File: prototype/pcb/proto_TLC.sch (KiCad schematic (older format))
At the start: 21 parts, among them U1 TLC5954

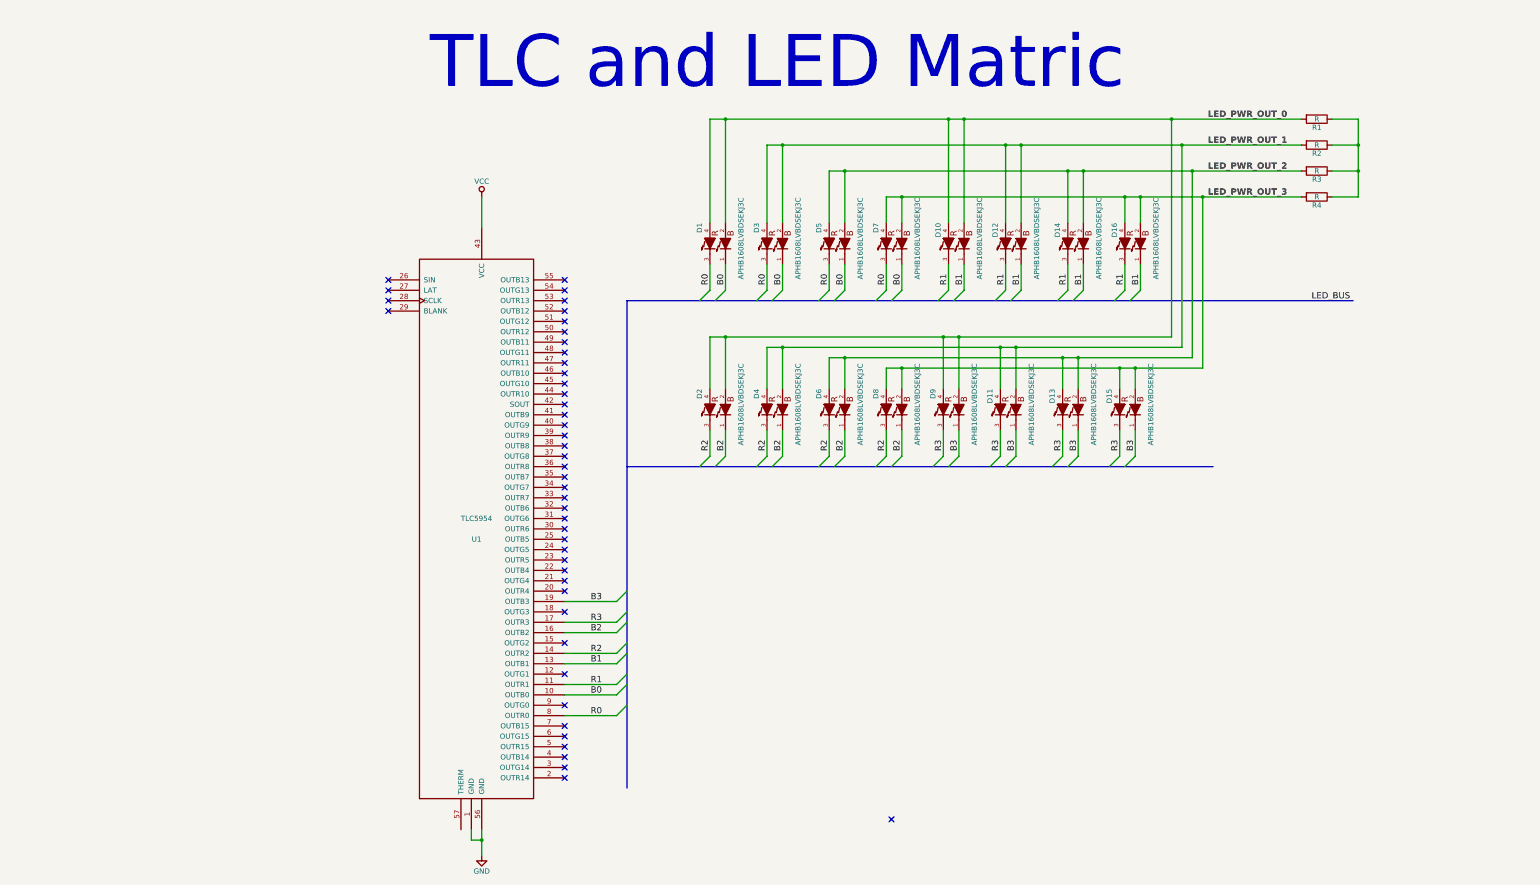
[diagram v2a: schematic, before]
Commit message: Added connectors, power mosfets, hierarchial pins
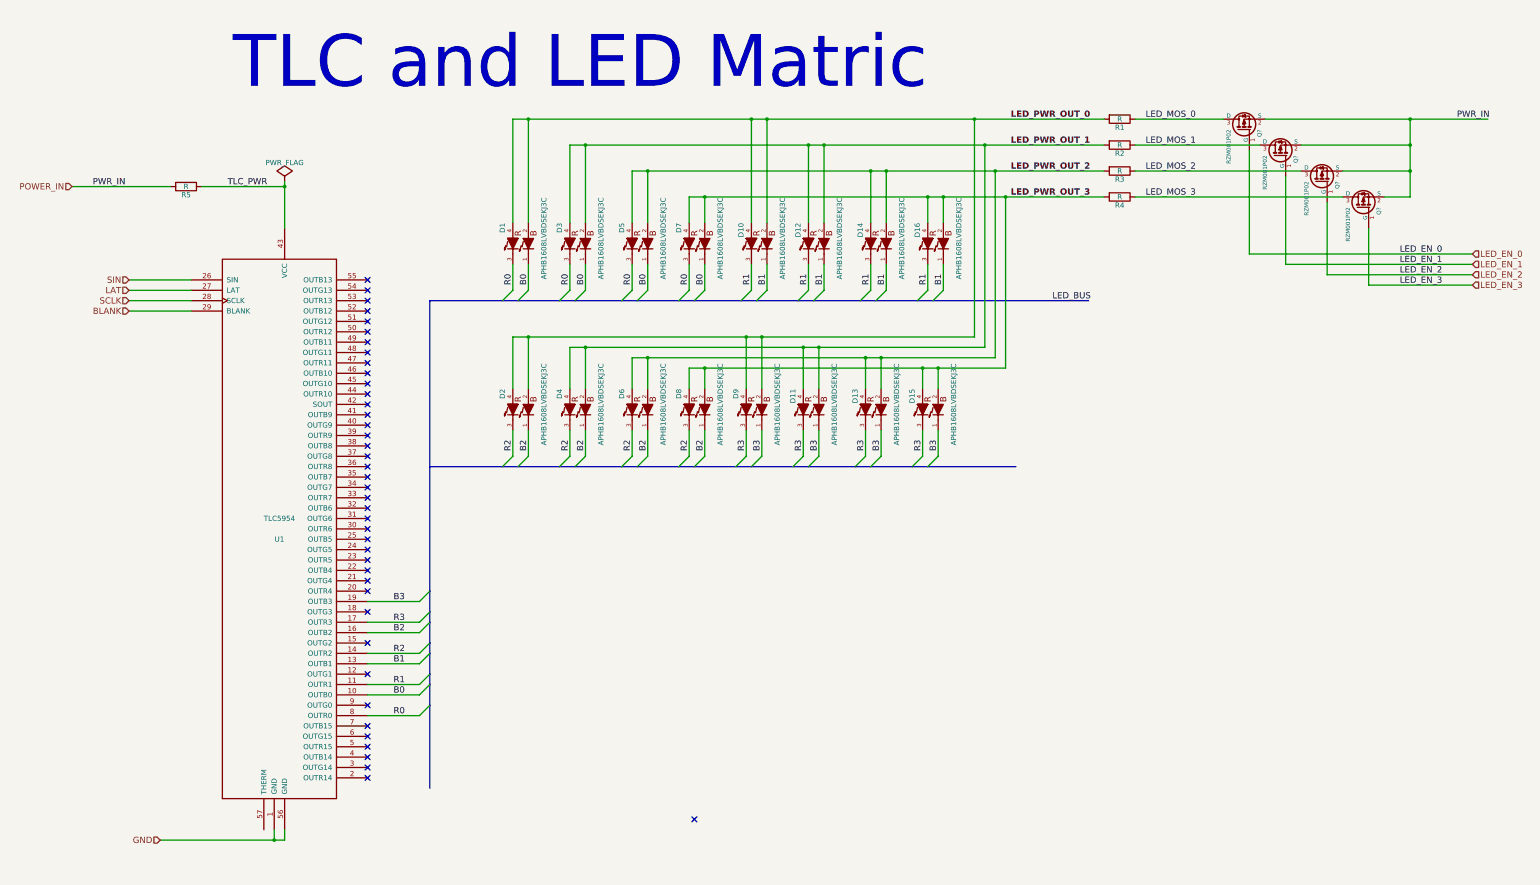
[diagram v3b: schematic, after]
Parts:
- added Q? (x4): RZM001P02, TO220, symbol RZM001P02
- added R5: R, symbol R
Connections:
- net SIN: now reaches U1.26 (SIN)
- net LAT: now reaches U1.27 (LAT)
- net SCLK: now reaches U1.28 (SCLK)
- net BLANK: now reaches U1.29 (BLANK)
- net VCC renamed TLC_PWR
- net TLC_PWR: now also R5.1
- new net LED_EN_0: Q?.1 (G)
- new net LED_EN_1: Q?.1 (G)
- new net LED_EN_2: Q?.1 (G)
- new net LED_EN_3: Q?.1 (G)
- new net LED_MOS_0: Q?.3 (D), R1.1
- new net LED_MOS_1: Q?.3 (D), R2.1
- new net LED_MOS_2: Q?.3 (D), R3.1
- new net LED_MOS_3: Q?.3 (D), R4.1
- new net POWER_IN: Q?.2 (S), Q?.2 (S), Q?.2 (S), Q?.2 (S), R5.2
- no-connect marks 46 -> 42
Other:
- moved on the sheet: D1, D10, D11, D12, D13, D14, D15, D16, D2, D3, D4, D5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

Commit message: Generate schematic pdf
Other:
- note added: "TLC and LED Matrix"
- note removed: "TLC and LED Matric"
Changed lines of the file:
@@
 $EndDescr
 Text Notes 3250 1400 0    500  ~ 0
-TLC and LED Matric
+TLC and LED Matrix
 $Comp
 L TLC5954 U1

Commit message: Bulk caps for TLC / LEDs
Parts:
- added C? (x3): C, symbol C
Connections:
- net GND: now also C?.2, C?.2, C?.2
- net POWER_IN: now also C?.1
- net TLC_PWR: now also C?.1, C?.1
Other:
- moved on the sheet: R5

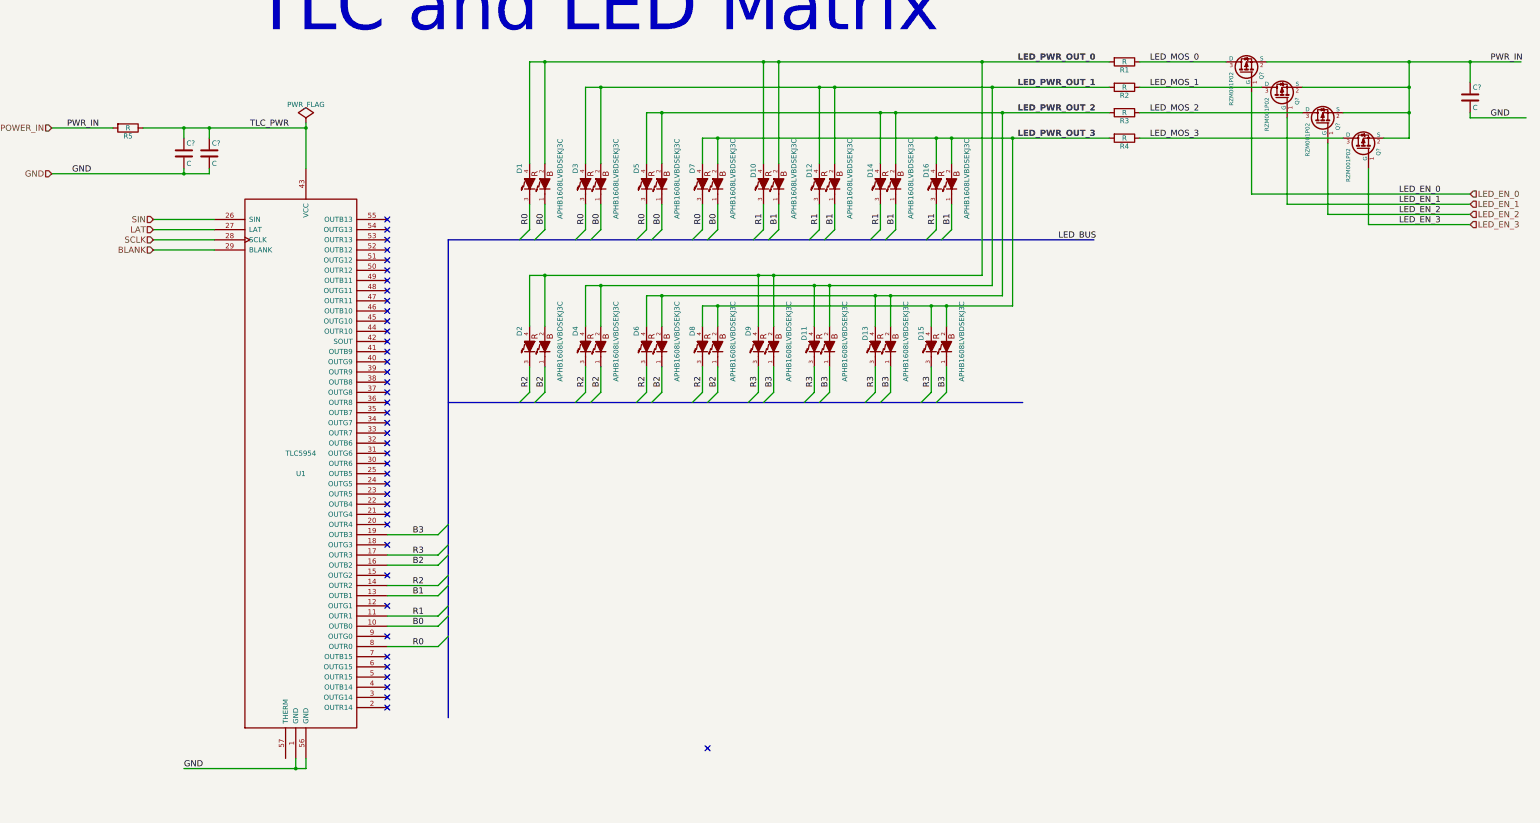
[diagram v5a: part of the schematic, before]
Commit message: Finished footprints and netlist
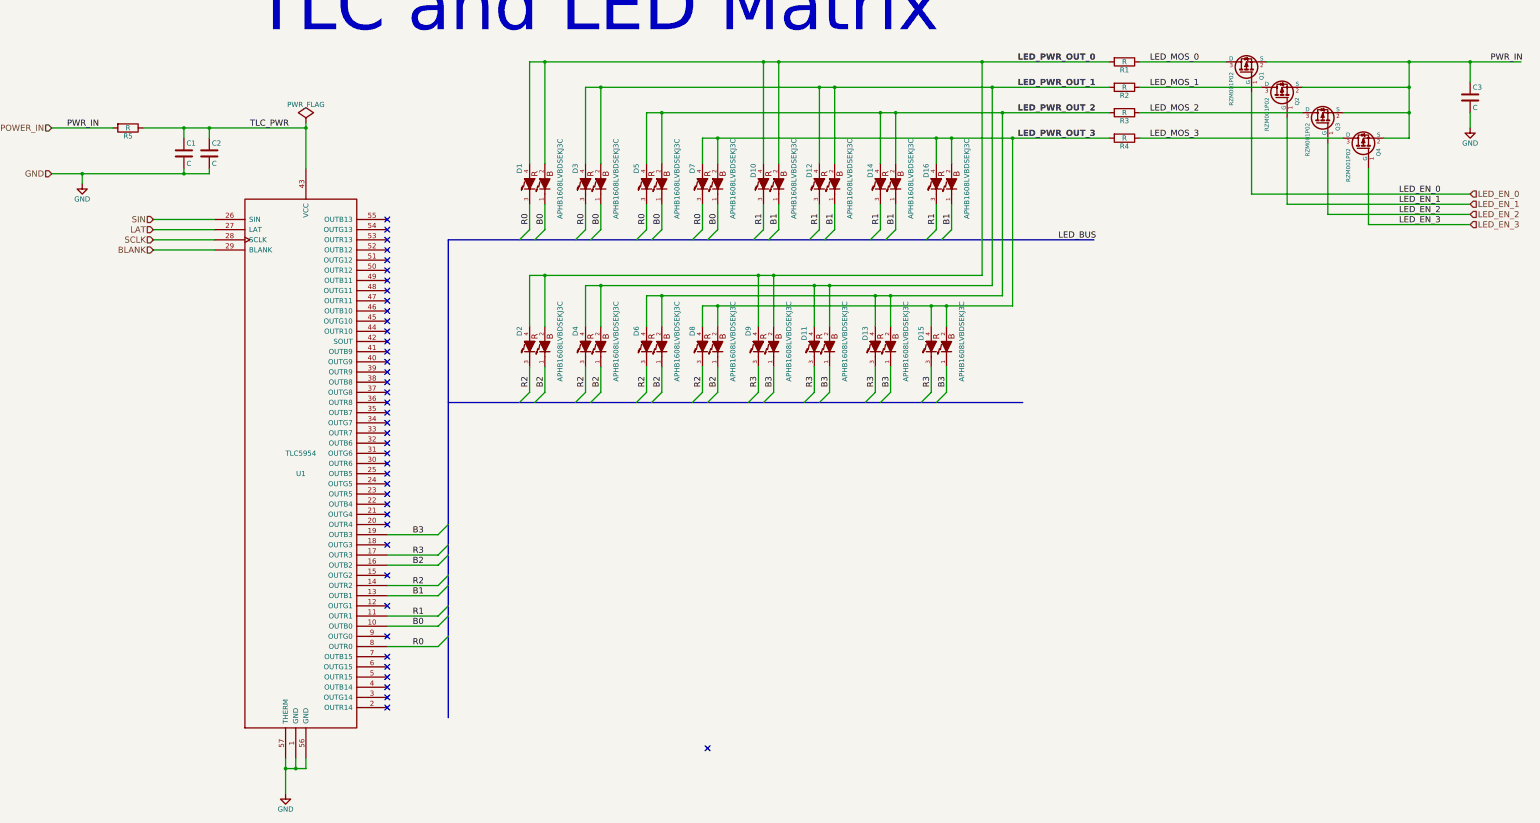
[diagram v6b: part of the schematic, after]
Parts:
- C1, C2, C3: renamed from C?; footprint (none) -> Capacitors_SMD:C_0603
- D1, D10, D11, D12, D13, D14, D15, D16, D2, D3, D4, D5, D6, D7, D8, D9: footprint (none) -> led:led_dual
- Q1, Q2, Q3, Q4: renamed from Q?; footprint TO220 -> smt:SOT-723-3
- R1, R2, R3, R4, R5: footprint (none) -> Resistors_SMD:R_0603
- U1: footprint MODULE -> smt:QFN_N56_THERM
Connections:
- net GND: now also U1.57 (THERM)
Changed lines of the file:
@@
 F 0 "U1" H 3700 5500 50  0000 C CNN
 F 1 "TLC5954" H 3700 5700 50  0000 C CNN
-F 2 "MODULE" H 3700 5600 50  0001 C CNN
+F 2 "smt:QFN_N56_THERM" H 3700 5600 50  0001 C CNN
 F 3 "DOCUMENTATION" H 3700 5600 50  0001 C CNN
 	1    3700 5600
@@
 F 0 "D1" H 5850 3050 50  0000 L CNN
 F 1 "APHB1608LVBDSEKJ3C" H 6000 2650 50  0000 C CNN
-F 2 "" H 6050 2800 60  0000 C CNN
+F 2 "led:led_dual" H 6050 2800 60  0001 C CNN
 F 3 "" H 6050 2800 60  0000 C CNN
 	1    6050 2850
@@
 F 0 "D3" H 6400 3050 50  0000 L CNN
 F 1 "APHB1608LVBDSEKJ3C" H 6550 2650 50  0000 C CNN
-F 2 "" H 6600 2800 60  0000 C CNN
+F 2 "led:led_dual" H 6600 2800 60  0001 C CNN
 F 3 "" H 6600 2800 60  0000 C CNN
 	1    6600 2850
@@
 F 0 "D5" H 7000 3050 50  0000 L CNN
 F 1 "APHB1608LVBDSEKJ3C" H 7150 2650 50  0000 C CNN
-F 2 "" H 7200 2800 60  0000 C CNN
+F 2 "led:led_dual" H 7200 2800 60  0001 C CNN
 F 3 "" H 7200 2800 60  0000 C CNN
 	1    7200 2850
@@
 F 0 "D7" H 7550 3050 50  0000 L CNN
 F 1 "APHB1608LVBDSEKJ3C" H 7700 2650 50  0000 C CNN
-F 2 "" H 7750 2800 60  0000 C CNN
+F 2 "led:led_dual" H 7750 2800 60  0001 C CNN
 F 3 "" H 7750 2800 60  0000 C CNN
 	1    7750 2850
@@
 F 0 "D10" H 8150 3050 50  0000 L CNN
 F 1 "APHB1608LVBDSEKJ3C" H 8300 2650 50  0000 C CNN
-F 2 "" H 8350 2800 60  0000 C CNN
+F 2 "led:led_dual" H 8350 2800 60  0001 C CNN
 F 3 "" H 8350 2800 60  0000 C CNN
 	1    8350 2850
@@
 F 0 "D12" H 8700 3050 50  0000 L CNN
 F 1 "APHB1608LVBDSEKJ3C" H 8850 2650 50  0000 C CNN
-F 2 "" H 8900 2800 60  0000 C CNN
+F 2 "led:led_dual" H 8900 2800 60  0001 C CNN
 F 3 "" H 8900 2800 60  0000 C CNN
 	1    8900 2850
@@
 F 0 "D14" H 9300 3050 50  0000 L CNN
 F 1 "APHB1608LVBDSEKJ3C" H 9450 2650 50  0000 C CNN
-F 2 "" H 9500 2800 60  0000 C CNN
+F 2 "led:led_dual" H 9500 2800 60  0001 C CNN
 F 3 "" H 9500 2800 60  0000 C CNN
 	1    9500 2850
@@
 F 0 "D16" H 9850 3050 50  0000 L CNN
 F 1 "APHB1608LVBDSEKJ3C" H 10000 2650 50  0000 C CNN
-F 2 "" H 10050 2800 60  0000 C CNN
+F 2 "led:led_dual" H 10050 2800 60  0001 C CNN
 F 3 "" H 10050 2800 60  0000 C CNN
 	1    10050 2850
@@
 F 0 "D2" H 5850 4650 50  0000 L CNN
 F 1 "APHB1608LVBDSEKJ3C" H 6000 4250 50  0000 C CNN
-F 2 "" H 6050 4400 60  0000 C CNN
+F 2 "led:led_dual" H 6050 4400 60  0001 C CNN
 F 3 "" H 6050 4400 60  0000 C CNN
 	1    6050 4450
@@
 F 0 "D4" H 6400 4650 50  0000 L CNN
 F 1 "APHB1608LVBDSEKJ3C" H 6550 4250 50  0000 C CNN
-F 2 "" H 6600 4400 60  0000 C CNN
+F 2 "led:led_dual" H 6600 4400 60  0001 C CNN
 F 3 "" H 6600 4400 60  0000 C CNN
 	1    6600 4450
@@
 F 0 "D6" H 7000 4650 50  0000 L CNN
 F 1 "APHB1608LVBDSEKJ3C" H 7150 4250 50  0000 C CNN
-F 2 "" H 7200 4400 60  0000 C CNN
+F 2 "led:led_dual" H 7200 4400 60  0001 C CNN
 F 3 "" H 7200 4400 60  0000 C CNN
 	1    7200 4450
@@
 F 0 "D8" H 7550 4650 50  0000 L CNN
 F 1 "APHB1608LVBDSEKJ3C" H 7700 4250 50  0000 C CNN
-F 2 "" H 7750 4400 60  0000 C CNN
+F 2 "led:led_dual" H 7750 4400 60  0001 C CNN
 F 3 "" H 7750 4400 60  0000 C CNN
 	1    7750 4450
@@
 F 0 "D9" H 8100 4650 50  0000 L CNN
 F 1 "APHB1608LVBDSEKJ3C" H 8250 4250 50  0000 C CNN
-F 2 "" H 8300 4400 60  0000 C CNN
+F 2 "led:led_dual" H 8300 4400 60  0001 C CNN
 F 3 "" H 8300 4400 60  0000 C CNN
 	1    8300 4450
@@
 F 0 "D11" H 8650 4650 50  0000 L CNN
 F 1 "APHB1608LVBDSEKJ3C" H 8800 4250 50  0000 C CNN
-F 2 "" H 8850 4400 60  0000 C CNN
+F 2 "led:led_dual" H 8850 4400 60  0001 C CNN
 F 3 "" H 8850 4400 60  0000 C CNN
 	1    8850 4450
@@
 F 0 "D13" H 9250 4650 50  0000 L CNN
 F 1 "APHB1608LVBDSEKJ3C" H 9400 4250 50  0000 C CNN
-F 2 "" H 9450 4400 60  0000 C CNN
+F 2 "led:led_dual" H 9450 4400 60  0001 C CNN
 F 3 "" H 9450 4400 60  0000 C CNN
 	1    9450 4450
@@
 F 0 "D15" H 9800 4650 50  0000 L CNN
 F 1 "APHB1608LVBDSEKJ3C" H 9950 4250 50  0000 C CNN
-F 2 "" H 10000 4400 60  0000 C CNN
+F 2 "led:led_dual" H 10000 4400 60  0001 C CNN
 F 3 "" H 10000 4400 60  0000 C CNN
 	1    10000 4450
@@
 F 0 "R4" V 11880 2400 50  0000 C CNN
 F 1 "R" V 11800 2400 50  0000 C CNN
-F 2 "" V 11730 2400 30  0000 C CNN
+F 2 "Resistors_SMD:R_0603" V 11730 2400 30  0001 C CNN
 F 3 "" H 11800 2400 30  0000 C CNN
 	1    11800 2400
@@
 F 0 "R1" V 11880 1650 50  0000 C CNN
 F 1 "R" V 11800 1650 50  0000 C CNN
-F 2 "" V 11730 1650 30  0000 C CNN
+F 2 "Resistors_SMD:R_0603" V 11730 1650 30  0001 C CNN
 F 3 "" H 11800 1650 30  0000 C CNN
 	1    11800 1650
@@
 F 0 "R2" V 11880 1900 50  0000 C CNN
 F 1 "R" V 11800 1900 50  0000 C CNN
-F 2 "" V 11730 1900 30  0000 C CNN
+F 2 "Resistors_SMD:R_0603" V 11730 1900 30  0001 C CNN
 F 3 "" H 11800 1900 30  0000 C CNN
 	1    11800 1900
@@
 F 0 "R3" V 11880 2150 50  0000 C CNN
 F 1 "R" V 11800 2150 50  0000 C CNN
-F 2 "" V 11730 2150 30  0000 C CNN
+F 2 "Resistors_SMD:R_0603" V 11730 2150 30  0001 C CNN
 F 3 "" H 11800 2150 30  0000 C CNN
 	1    11800 2150
@@
 F 0 "R5" V 2080 2300 50  0000 C CNN
 F 1 "R" V 2000 2300 50  0000 C CNN
-F 2 "" V 1930 2300 30  0000 C CNN
+F 2 "Resistors_SMD:R_0603" V 1930 2300 30  0001 C CNN
 F 3 "" H 2000 2300 30  0000 C CNN
 	1    2000 2300
@@
 GND
 Wire Wire Line
-	2550 8600 3750 8600
+	3550 8600 3750 8600
 Wire Wire Line
 	3750 8600 3750 8500
-Wire Wire Line
-	3650 8500 3650 8600
 Connection ~ 3650 8600
 $Comp
@@
 Connection ~ 3750 2300
 $Comp
-L RZM001P02 Q?
+L RZM001P02 Q1
 U 1 1 574F2CDF
 P 13000 1750
-F 0 "Q?" H 13000 1602 40  0000 R CNN
+F 0 "Q1" H 13000 1602 40  0000 R CNN
 F 1 "RZM001P02" H 13000 1899 40  0000 R CNN
-F 2 "TO220" H 12781 1851 29  0001 C CNN
+F 2 "smt:SOT-723-3" H 12781 1851 29  0001 C CNN
 F 3 "" H 13000 1750 60  0000 C CNN
 	1    13000 1750
@@
 $EndComp
 $Comp
-L RZM001P02 Q?
+L RZM001P02 Q2
 U 1 1 574F3320
 P 13350 2000
-F 0 "Q?" H 13350 1852 40  0000 R CNN
+F 0 "Q2" H 13350 1852 40  0000 R CNN
 F 1 "RZM001P02" H 13350 2149 40  0000 R CNN
-F 2 "TO220" H 13131 2101 29  0001 C CNN
+F 2 "smt:SOT-723-3" H 13131 2101 29  0001 C CNN
 F 3 "" H 13350 2000 60  0000 C CNN
 	1    13350 2000
@@
 $EndComp
 $Comp
-L RZM001P02 Q?
+L RZM001P02 Q3
 U 1 1 574F337A
 P 13750 2250
-F 0 "Q?" H 13750 2102 40  0000 R CNN
+F 0 "Q3" H 13750 2102 40  0000 R CNN
 F 1 "RZM001P02" H 13750 2399 40  0000 R CNN
-F 2 "TO220" H 13531 2351 29  0001 C CNN
+F 2 "smt:SOT-723-3" H 13531 2351 29  0001 C CNN
 F 3 "" H 13750 2250 60  0000 C CNN
 	1    13750 2250
@@
 $EndComp
 $Comp
-L RZM001P02 Q?
+L RZM001P02 Q4
 U 1 1 574F3564
 P 14150 2500
-F 0 "Q?" H 14150 2352 40  0000 R CNN
+F 0 "Q4" H 14150 2352 40  0000 R CNN
 F 1 "RZM001P02" H 14150 2649 40  0000 R CNN
-F 2 "TO220" H 13931 2601 29  0001 C CNN
+F 2 "smt:SOT-723-3" H 13931 2601 29  0001 C CNN
 F 3 "" H 14150 2500 60  0000 C CNN
 	1    14150 2500
@@
 LED_EN_3
 $Comp
-L C C?
+L C C1
 U 1 1 574F4CFC
 P 2550 2550
-F 0 "C?" H 2575 2650 50  0000 L CNN
+F 0 "C1" H 2575 2650 50  0000 L CNN
 F 1 "C" H 2575 2450 50  0000 L CNN
-F 2 "" H 2588 2400 30  0000 C CNN
+F 2 "Capacitors_SMD:C_0603" H 2588 2400 30  0001 C CNN
 F 3 "" H 2550 2550 60  0000 C CNN
 	1    2550 2550
@@
 	2550 2400 2550 2300
 Connection ~ 2550 2300
-Text Label 2550 8600 0    60   ~ 0
-GND
 Wire Wire Line
 	1250 2750 2800 2750
 Wire Wire Line
 	2550 2750 2550 2700
-Text Label 1450 2750 0    60   ~ 0
-GND
-$Comp
-L C C?
+$Comp
+L C C2
 U 1 1 574F5C22
 P 2800 2550
-F 0 "C?" H 2825 2650 50  0000 L CNN
+F 0 "C2" H 2825 2650 50  0000 L CNN
 F 1 "C" H 2825 2450 50  0000 L CNN
-F 2 "" H 2838 2400 30  0000 C CNN
+F 2 "Capacitors_SMD:C_0603" H 2838 2400 30  0001 C CNN
 F 3 "" H 2800 2550 60  0000 C CNN
 	1    2800 2550
@@
 Connection ~ 2550 2750
 $Comp
-L C C?
+L C C3
 U 1 1 574F60F7
 P 15200 2000
-F 0 "C?" H 15225 2100 50  0000 L CNN
+F 0 "C3" H 15225 2100 50  0000 L CNN
 F 1 "C" H 15225 1900 50  0000 L CNN
-F 2 "" H 15238 1850 30  0000 C CNN
+F 2 "Capacitors_SMD:C_0603" H 15238 1850 30  0001 C CNN
 F 3 "" H 15200 2000 60  0000 C CNN
 	1    15200 2000
@@
 Connection ~ 15200 1650
 Wire Wire Line
-	15200 2150 15200 2200
-Wire Wire Line
-	15200 2200 15750 2200
-Text Label 15400 2200 0    60   ~ 0
-GND
+	15200 2150 15200 2300
+$Comp
+L GND #PWR07
+U 1 1 574F686D
+P 15200 2300
+F 0 "#PWR07" H 15200 2050 50  0001 C CNN
+F 1 "GND" H 15200 2150 50  0000 C CNN
+F 2 "" H 15200 2300 60  0000 C CNN
+F 3 "" H 15200 2300 60  0000 C CNN
+	1    15200 2300
+	1    0    0    -1
+$EndComp
+$Comp
+L GND #PWR08
+U 1 1 574F6FFB
+P 3550 8850
+F 0 "#PWR08" H 3550 8600 50  0001 C CNN
+F 1 "GND" H 3550 8700 50  0000 C CNN
+F 2 "" H 3550 8850 60  0000 C CNN
+F 3 "" H 3550 8850 60  0000 C CNN
+	1    3550 8850
+	1    0    0    -1
+$EndComp
+$Comp
+L GND #PWR09
+U 1 1 574F75CF
+P 1550 2850
+F 0 "#PWR09" H 1550 2600 50  0001 C CNN
+F 1 "GND" H 1550 2700 50  0000 C CNN
+F 2 "" H 1550 2850 60  0000 C CNN
+F 3 "" H 1550 2850 60  0000 C CNN
+	1    1550 2850
+	1    0    0    -1
+$EndComp
+Wire Wire Line
+	1550 2850 1550 2750
+Connection ~ 1550 2750
+Wire Wire Line
+	3550 8500 3550 8850
+Connection ~ 3550 8600
+Wire Wire Line
+	3650 8500 3650 8600
 $EndSCHEMATC
